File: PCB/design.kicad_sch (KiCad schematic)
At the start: 5 parts, among them U3 NUCLEO-L432KC

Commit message: add better ground vias; rename footprints and 3d-models
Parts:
- G1, G2, G3, G4: footprint customLib:rubber-feet -> customLib:G2009
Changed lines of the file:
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@@
 			)
 		)
-		(property "Footprint" "customLib:rubber-feet"
+		(property "Footprint" "customLib:G2009"
 			(at 123.19 148.59 0)
 			(effects
@@
 			)
 		)
-		(property "Footprint" "customLib:rubber-feet"
+		(property "Footprint" "customLib:G2009"
 			(at 128.27 143.51 0)
 			(effects
@@
 			)
 		)
-		(property "Footprint" "customLib:rubber-feet"
+		(property "Footprint" "customLib:G2009"
 			(at 123.19 143.51 0)
 			(effects
@@
 			)
 		)
-		(property "Footprint" "customLib:rubber-feet"
+		(property "Footprint" "customLib:G2009"
 			(at 128.27 148.59 0)
 			(effects

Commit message: remove unneeded pin; update invalid footprint
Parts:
- U3: footprint customLib:MODULE_NUCLEO-L432KC -> customLib:NUCLEO-L432KC
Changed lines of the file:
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@@
 			)
 		)
-		(property "Footprint" "customLib:MODULE_NUCLEO-L432KC"
+		(property "Footprint" "customLib:NUCLEO-L432KC"
 			(at 187.96 97.79 0)
 			(effects
@@
 			)
 		)
-		(property "Footprint" "customLib:MODULE_NUCLEO-L432KC"
+		(property "Footprint" "customLib:NUCLEO-L432KC"
 			(at 144.78 97.79 0)
 			(effects

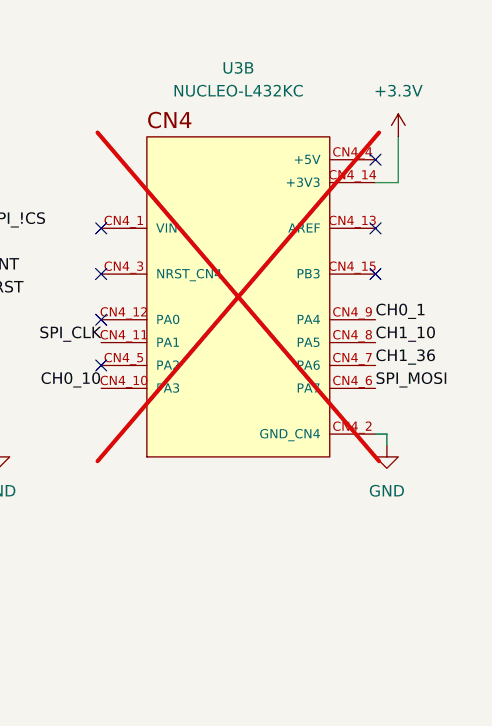
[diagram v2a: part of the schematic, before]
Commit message: resolve symbol, footprint issues
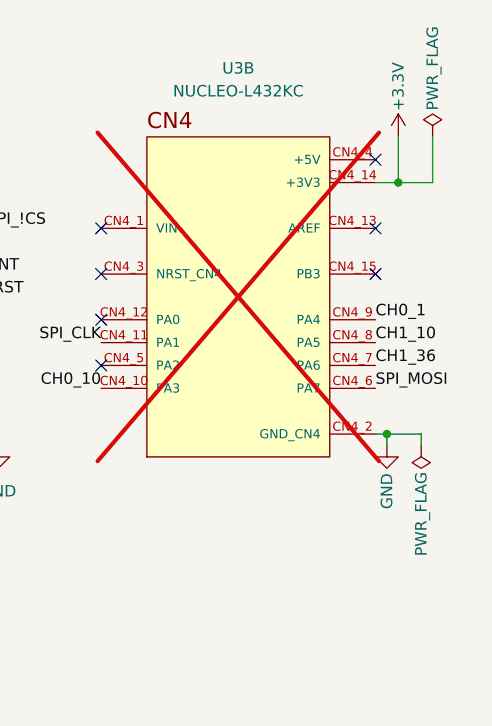
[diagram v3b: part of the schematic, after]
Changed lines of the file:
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@@
 		)
+	)
+	(junction
+		(at 205.74 85.09)
+		(diameter 0)
+		(color 0 0 0 0)
+	)
+	(junction
+		(at 204.47 113.03)
+		(diameter 0)
+		(color 0 0 0 0)
 	)
 	(no_connect
@@
 	(wire
 		(pts
-			(xy 160.02 113.03) (xy 161.29 113.03)
+			(xy 208.28 113.03) (xy 208.28 114.3)
 		)
 		(stroke
@@
 	(wire
 		(pts
-			(xy 205.74 85.09) (xy 205.74 80.01)
+			(xy 160.02 113.03) (xy 161.29 113.03)
 		)
 		(stroke
@@
 	(wire
 		(pts
-			(xy 204.47 113.03) (xy 204.47 114.3)
+			(xy 204.47 113.03) (xy 208.28 113.03)
 		)
 		(stroke
@@
 	(wire
 		(pts
-			(xy 203.2 85.09) (xy 205.74 85.09)
+			(xy 209.55 85.09) (xy 209.55 80.01)
 		)
 		(stroke
@@
 	(wire
 		(pts
-			(xy 203.2 113.03) (xy 204.47 113.03)
+			(xy 204.47 113.03) (xy 203.2 113.03)
+		)
+		(stroke
+			(width 0)
+			(type default)
+		)
+	)
+	(wire
+		(pts
+			(xy 205.74 85.09) (xy 205.74 80.01)
+		)
+		(stroke
+			(width 0)
+			(type default)
+		)
+	)
+	(wire
+		(pts
+			(xy 205.74 85.09) (xy 209.55 85.09)
+		)
+		(stroke
+			(width 0)
+			(type default)
+		)
+	)
+	(wire
+		(pts
+			(xy 204.47 113.03) (xy 204.47 114.3)
+		)
+		(stroke
+			(width 0)
+			(type default)
+		)
+	)
+	(wire
+		(pts
+			(xy 203.2 85.09) (xy 205.74 85.09)
 		)
 		(stroke
@@
 	)
 	(symbol
+		(lib_id "power:PWR_FLAG")
+		(at 208.28 114.3 180)
+		(unit 1)
+		(exclude_from_sim no)
+		(in_bom yes)
+		(on_board yes)
+		(dnp no)
+		(property "Reference" "#FLG02"
+			(at 208.28 116.205 0)
+			(effects
+				(font
+					(size 1.27 1.27)
+				)
+				(hide yes)
+			)
+		)
+		(property "Value" "PWR_FLAG"
+			(at 208.28 121.92 90)
+			(effects
+				(font
+					(size 1.27 1.27)
+				)
+			)
+		)
+		(property "Footprint" ""
+			(at 208.28 114.3 0)
+			(effects
+				(font
+					(size 1.27 1.27)
+				)
+				(hide yes)
+			)
+		)
+		(property "Datasheet" "~"
+			(at 208.28 114.3 0)
+			(effects
+				(font
+					(size 1.27 1.27)
+				)
+				(hide yes)
+			)
+		)
+		(property "Description" "Special symbol for telling ERC where power comes from"
+			(at 208.28 114.3 0)
+			(effects
+				(font
+					(size 1.27 1.27)
+				)
+				(hide yes)
+			)
+		)
+		(pin "1"
+		)
+		(instances
+			(project "design"
+				(path "/b7c29cd9-215b-4083-930c-731c0fdbf2f7"
+					(reference "#FLG02")
+					(unit 1)
+				)
+			)
+		)
+	)
+	(symbol
+		(lib_id "power:PWR_FLAG")
+		(at 209.55 80.01 0)
+		(unit 1)
+		(exclude_from_sim no)
+		(in_bom yes)
+		(on_board yes)
+		(dnp no)
+		(property "Reference" "#FLG01"
+			(at 209.55 78.105 0)
+			(effects
+				(font
+					(size 1.27 1.27)
+				)
+				(hide yes)
+			)
+		)
+		(property "Value" "PWR_FLAG"
+			(at 209.55 72.39 90)
+			(effects
+				(font
+					(size 1.27 1.27)
+				)
+			)
+		)
+		(property "Footprint" ""
+			(at 209.55 80.01 0)
+			(effects
+				(font
+					(size 1.27 1.27)
+				)
+				(hide yes)
+			)
+		)
+		(property "Datasheet" "~"
+			(at 209.55 80.01 0)
+			(effects
+				(font
+					(size 1.27 1.27)
+				)
+				(hide yes)
+			)
+		)
+		(property "Description" "Special symbol for telling ERC where power comes from"
+			(at 209.55 80.01 0)
+			(effects
+				(font
+					(size 1.27 1.27)
+				)
+				(hide yes)
+			)
+		)
+		(pin "1"
+		)
+		(instances
+			(project ""
+				(path "/b7c29cd9-215b-4083-930c-731c0fdbf2f7"
+					(reference "#FLG01")
+					(unit 1)
+				)
+			)
+		)
+	)
+	(symbol
 		(lib_id "power:+3.3V")
 		(at 205.74 80.01 0)
@@
 		(on_board yes)
 		(dnp no)
-		(fields_autoplaced yes)
 		(property "Reference" "#PWR047"
 			(at 205.74 83.82 0)
@@
 		)
 		(property "Value" "+3.3V"
-			(at 205.74 74.93 0)
+			(at 205.74 74.422 90)
 			(effects
 				(font
@@
 		(on_board yes)
 		(dnp no)
-		(fields_autoplaced yes)
 		(property "Reference" "#PWR024"
 			(at 204.47 120.65 0)
@@
 		)
 		(property "Value" "GND"
-			(at 204.47 119.38 0)
-			(effects
-				(font
+			(at 204.47 119.38 90)
+			(effects
+				(font
